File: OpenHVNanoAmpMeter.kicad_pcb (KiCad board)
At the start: 2 copper layers, 7 parts, among them U1 DDC112U

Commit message: started some layouting
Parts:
- added J1: Conn_Coaxial, Connector_Coaxial:SMA_Amphenol_132289_EdgeMount, F.Cu at (56.2, 61.9)
- added J2: Conn_Coaxial, Connector_Coaxial:SMA_Amphenol_132289_EdgeMount, F.Cu at (56.2, 42.9)
- added J3: AVR-ISP-6, Connector_PinHeader_2.54mm:PinHeader_2x03_P2.54mm_Vertical_SMD, F.Cu at (100.0, 57.0)
- added R1: R, Resistor_SMD:R_0603_1608Metric, F.Cu at (60.9, 59.9)
- added R2: R, Resistor_SMD:R_0603_1608Metric, F.Cu at (60.9, 44.9)
- added R3: 4k7, Resistor_SMD:R_0603_1608Metric, F.Cu at (94.3, 62.7)
- added R4: 4k7, Resistor_SMD:R_0402_1005Metric, F.Cu at (104.8, 69.0)
- added R5: 4k7, Resistor_SMD:R_0402_1005Metric, F.Cu at (104.8, 68.1)
- added R6: 4k7, Resistor_SMD:R_0402_1005Metric, F.Cu at (104.8, 70.0)
- added R7: 4k7, Resistor_SMD:R_0402_1005Metric, F.Cu at (104.8, 67.1)
- added U2: ATmega328PB-M, Package_DFN_QFN:QFN-32-1EP_5x5mm_P0.5mm_EP3.1x3.1mm, F.Cu at (92.3, 45.8)
- added U3: 74LV8154, Package_SO:TSSOP-20_4.4x6.5mm_P0.65mm, F.Cu at (99.0, 66.9)
- added U4: 74LS151, Package_SO:SO-16_3.9x9.9mm_P1.27mm, F.Cu at (87.8, 65.3)
- added X1: ASCO, Oscillator:Oscillator_SMD_Abracon_ASCO-4Pin_1.6x1.2mm, F.Cu at (105.0, 65.5)
- moved C4 146.4 mm to (64.1, 45.9), turned to 180 degrees
- moved C3 145.0 mm to (66.6, 45.9), turned to 180 degrees
- moved U1 135.1 mm to (69.2, 52.4), turned to 90 degrees
- moved C2 129.9 mm to (64.1, 58.9), turned to 0 degrees
- moved C1 128.3 mm to (66.6, 58.9), turned to 0 degrees
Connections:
- U1 pad 1: /CurrentMeasurement/IN1 -> Net-(R1-Pad2)
- U1 pad 10: unconnected-(U1-Pad10) -> /Clock Generation/CLK_10MHz
- U1 pad 11: unconnected-(U1-Pad11) -> /CurrentMeasurement/DCLK
- U1 pad 12: unconnected-(U1-Pad12) -> /CurrentMeasurement/DXMIT
- U1 pad 13: unconnected-(U1-Pad13) -> /CurrentMeasurement/DIN
- U1 pad 16: unconnected-(U1-Pad16) -> /CurrentMeasurement/DOUT
- U1 pad 17: unconnected-(U1-Pad17) -> /CurrentMeasurement/DVALID
- U1 pad 18: unconnected-(U1-Pad18) -> /CurrentMeasurement/RANGE0
- U1 pad 19: unconnected-(U1-Pad19) -> /CurrentMeasurement/RANGE1
- U1 pad 20: unconnected-(U1-Pad20) -> /CurrentMeasurement/RANGE2
- U1 pad 22: unconnected-(U1-Pad22) -> /CurrentMeasurement/VREF
- U1 pad 28: /CurrentMeasurement/IN2 -> Net-(R2-Pad2)
- U1 pad 8: unconnected-(U1-Pad8) -> /CurrentMeasurement/TEST
- U1 pad 9: unconnected-(U1-Pad9) -> /Clock Generation/CONV
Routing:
- net /Clock Generation/BIT3: track 0.00 -> 11.8 mm, vias 0 -> 2
- net /Clock Generation/BIT2: track 0.00 -> 11.6 mm, vias 0 -> 2
- net /Clock Generation/BIT1: track 0.00 -> 11.5 mm, vias 0 -> 2
- net /Clock Generation/BIT0: track 0.00 -> 11.4 mm, vias 0 -> 2
- net /Clock Generation/BIT4: track 0.00 -> 8.55 mm
- net /Clock Generation/BIT5: track 0.00 -> 7.63 mm
- net /Clock Generation/BIT6: track 0.00 -> 6.57 mm
- net /Clock Generation/BIT7: track 0.00 -> 6.31 mm
- net /CurrentMeasurement/IN2: track 0.00 -> 5.76 mm
- net /CurrentMeasurement/IN1: track 0.00 -> 5.73 mm
- net Net-(R2-Pad2): track 0.00 -> 2.02 mm
- net Net-(R1-Pad2): track 0.00 -> 2.02 mm
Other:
- board outline added: 75.9 x 39.3 mm

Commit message: proceeded with routing
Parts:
- removed BT2: 9V, Battery:BatteryHolder_MPD_BA9VPC_1xPP3
- added C10: 10u, Capacitor_SMD:CP_Elec_4x3.9, F.Cu at (78.6, 63.3)
- added C11: 100n, Capacitor_SMD:C_0603_1608Metric, F.Cu at (76.8, 59.1)
- added C12: 100n, Capacitor_SMD:C_0603_1608Metric, F.Cu at (85.1, 56.3)
- added C13: 100n, Capacitor_SMD:C_0603_1608Metric, F.Cu at (83.6, 56.3)
- added C14: 100n, Capacitor_SMD:C_0603_1608Metric, F.Cu at (85.4, 46.3)
- added C15: 100n, Capacitor_SMD:C_0603_1608Metric, F.Cu at (93.9, 71.0)
- added C16: 100n, Capacitor_SMD:C_0603_1608Metric, F.Cu at (82.9, 71.0)
- added C17: 100n, Capacitor_SMD:C_0603_1608Metric, F.Cu at (104.6, 70.6)
- added C5: 10u, Capacitor_SMD:CP_Elec_4x3.9, F.Cu at (81.5, 15.4)
- added C6: 100n, Capacitor_SMD:C_0603_1608Metric, F.Cu at (79.2, 19.0)
- added C7: 470n, Capacitor_SMD:C_0603_1608Metric, F.Cu at (71.1, 17.4)
- added C8: 10u, Capacitor_SMD:CP_Elec_4x3.9, F.Cu at (68.6, 63.3)
- added C9: 100n, Capacitor_SMD:C_0603_1608Metric, F.Cu at (69.4, 59.1)
- added R8: 10k, Resistor_SMD:R_0603_1608Metric, F.Cu at (77.0, 18.2)
- added U5: REF3040, Package_TO_SOT_SMD:SOT-23, F.Cu at (73.7, 17.2)
- BT1: moved to B.Cu
- moved BT1 58.6 mm to (113.8, 45.8), turned to 180 degrees
- moved J3 14.4 mm to (95.3, 43.4)
- moved U2 8.99 mm to (85.1, 51.3), turned to -90 degrees
- moved X1 5.63 mm to (101.9, 70.2)
- moved R4 3.33 mm to (101.7, 67.8)
- moved R5 3.33 mm to (101.7, 66.8)
- moved R6 3.33 mm to (101.7, 68.7)
- moved R7 3.33 mm to (101.7, 65.8)
- moved R3 2.98 mm to (91.4, 62.5)
- moved U4 2.98 mm to (84.8, 65.0)
- moved U3 2.98 mm to (96.1, 66.6)
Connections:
- BT1 pad 2: Net-(BT1-Pad2) -> unconnected-(BT1-Pad2)
- J3 pad 2: unconnected-(J3-Pad2) -> +5VD
- R6 pad 1: Net-(R6-Pad1) -> +5VD
- R7 pad 1: Net-(R6-Pad1) -> +5VD
- U1 pad 13: /CurrentMeasurement/DIN -> GND
- U1 pad 14: unconnected-(U1-Pad14) -> +5VD
- U1 pad 7: unconnected-(U1-Pad7) -> +5VA
- U2 pad 18: Net-(U2-Pad18) -> +5VD
- U2 pad 20: Net-(U2-Pad18) -> +5VD
- U2 pad 22: /CurrentMeasurement/DIN -> unconnected-(U2-Pad22)
- U2 pad 4: Net-(U2-Pad18) -> +5VD
- U3 pad 20: unconnected-(U3-Pad20) -> +5VD
- U4 pad 16: unconnected-(U4-Pad16) -> +5VD
- X1 pad 4: unconnected-(X1-Pad4) -> +5VD
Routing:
- net /Clock Generation/MUX_S0: track 0.00 -> 28.3 mm, vias 0 -> 2
- net /Clock Generation/MUX_S1: track 0.00 -> 25.7 mm, vias 0 -> 2
- net /Clock Generation/MUX_S2: track 0.00 -> 23.3 mm, vias 0 -> 2
- net +5VD: track 0.00 -> 22.7 mm, vias 0 -> 2
- net /Clock Generation/CONV: track 0.00 -> 16.9 mm
- net /CurrentMeasurement/RANGE2: track 0.00 -> 13.8 mm
- net /CurrentMeasurement/RANGE1: track 0.00 -> 12.3 mm
- net /Clock Generation/CLK_10MHz: track 0.00 -> 11.7 mm, vias 0 -> 1
- net /DataProcessing/~{RESET}: track 0.00 -> 10.8 mm
- net /CurrentMeasurement/RANGE0: track 0.00 -> 10.6 mm
- net /DataProcessing/SCL: track 0.00 -> 7.85 mm
- net /DataProcessing/SDA: track 0.00 -> 7.74 mm
- net /DataProcessing/TXD0: track 0.00 -> 7.41 mm
- net /DataProcessing/RXD0: track 0.00 -> 7.35 mm
- net +5VA: track 0.00 -> 5.13 mm
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- added copper zone on B.Cu, net GND
- added copper zone on F.Cu, net GND
- added copper zone on B.Cu, net GNDA
- added copper zone on F.Cu, net GNDA
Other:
- board size 75.9 x 39.3 mm -> 64.5 x 38 mm
- board text added: "IN1"
- board text added: "IN2"

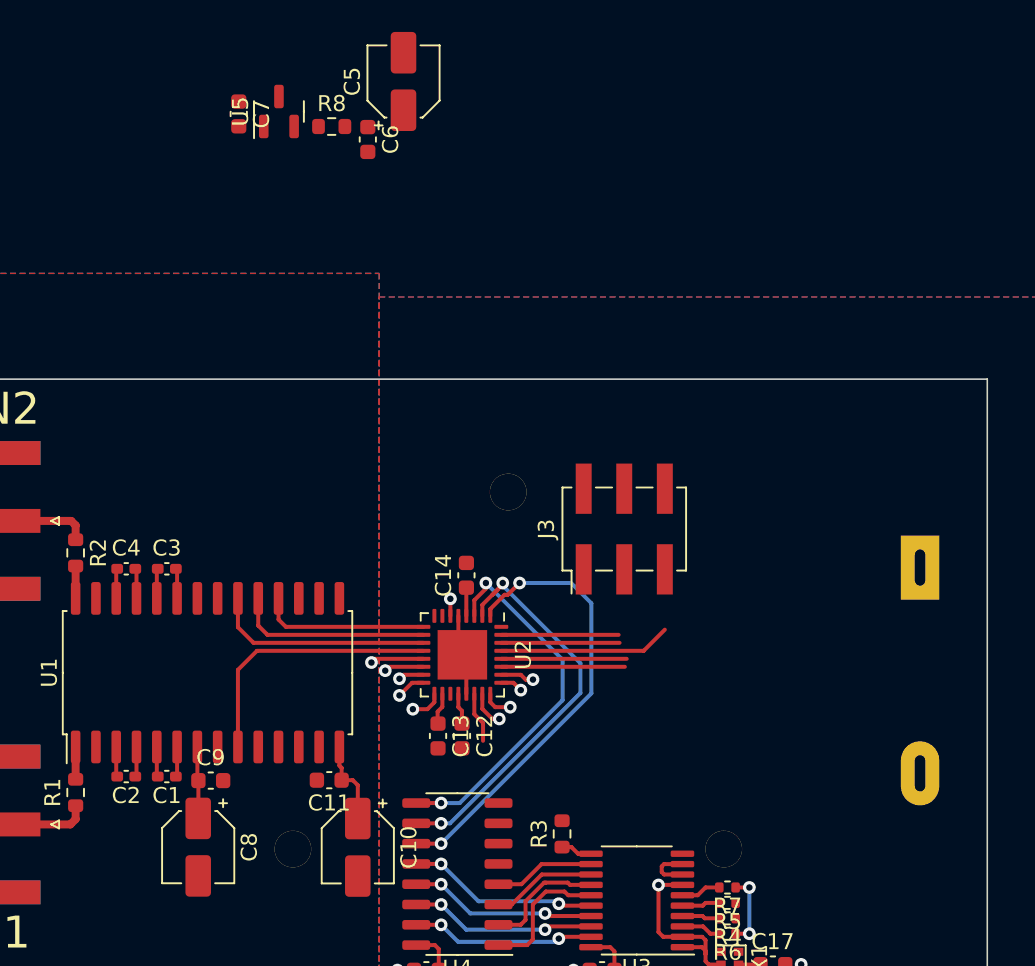
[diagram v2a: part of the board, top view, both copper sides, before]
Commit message: ISP connection routed
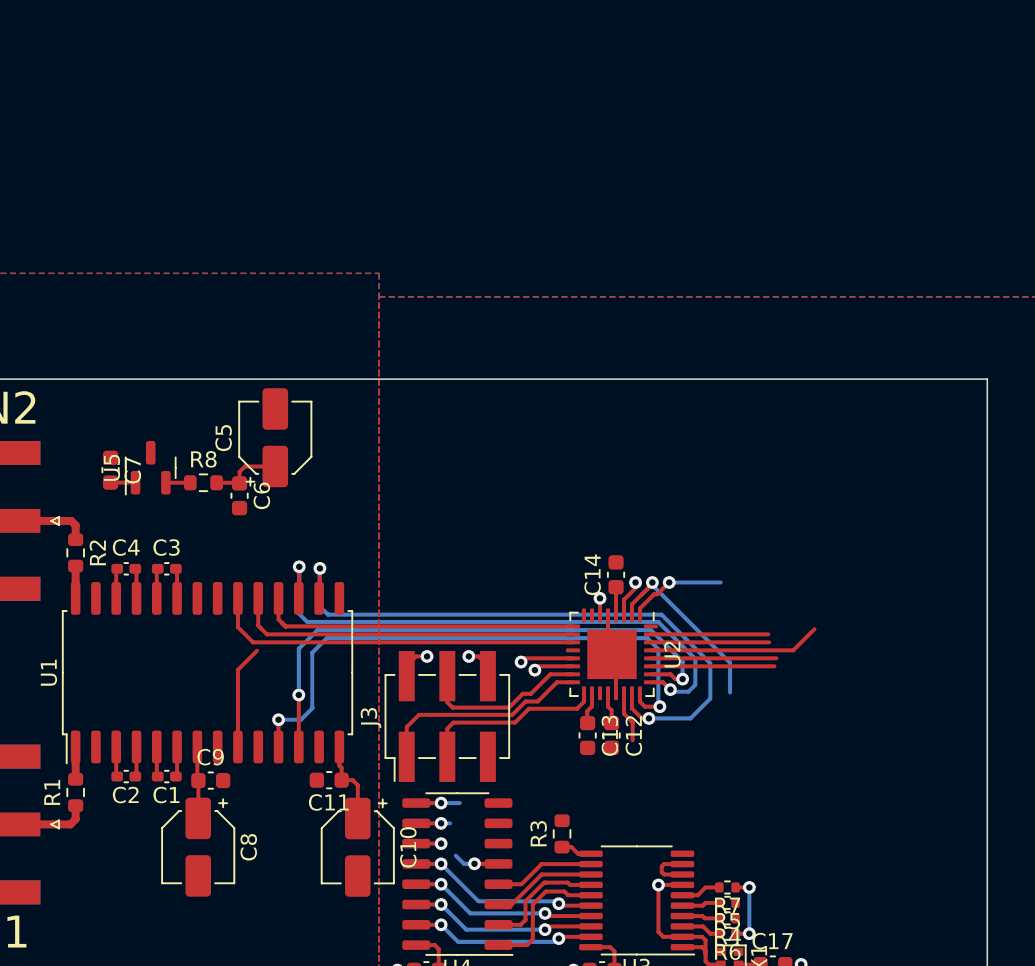
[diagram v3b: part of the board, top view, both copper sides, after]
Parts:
- removed BT1: 9V, Battery:BatteryHolder_MPD_BA9VPC_1xPP3
- moved R8 23.7 mm to (68.9, 40.5)
- moved C5 23.7 mm to (73.4, 37.7)
- moved C6 23.7 mm to (71.2, 41.3)
- moved C7 23.7 mm to (63.1, 39.7)
- moved U5 23.7 mm to (65.6, 39.5)
- moved J3 16.1 mm to (84.2, 55.1)
- moved C12 9.37 mm to (94.5, 56.3)
- moved C13 9.37 mm to (93.0, 56.3)
- moved C14 9.37 mm to (94.8, 46.2)
- moved U2 9.37 mm to (94.5, 51.2)
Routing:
- net /CurrentMeasurement/DOUT: track 2.27 -> 39.0 mm, vias 1 -> 2
- net /CurrentMeasurement/DVALID: track 1.41 -> 35.7 mm, vias 1 -> 2
- net /CurrentMeasurement/DCLK: track 1.91 -> 35.5 mm, vias 1 -> 2
- net /CurrentMeasurement/DXMIT: track 2.11 -> 35.3 mm, vias 1 -> 2
- net /Clock Generation/MUX_S0: track 28.3 -> 7.54 mm
- net /Clock Generation/MUX_S2: track 23.3 -> 4.91 mm
- net /Clock Generation/MUX_S1: track 25.7 -> 14.0 mm
- net /DataProcessing/MISO: track 1.83 -> 13.4 mm, vias 1 -> 0
- net /CurrentMeasurement/RANGE0: track 10.6 -> 20.3 mm
- net /DataProcessing/SCK: track 2.06 -> 11.5 mm, vias 1 -> 0
- net /CurrentMeasurement/RANGE2: track 13.8 -> 23.2 mm
- net /CurrentMeasurement/RANGE1: track 12.3 -> 21.6 mm
- net /DataProcessing/MOSI: track 1.60 -> 10.5 mm, vias 1 -> 0
- net /Clock Generation/CONV: track 16.9 -> 9.39 mm, vias 0 -> 1
- net Net-(C5-Pad1): track 0.00 -> 4.55 mm
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
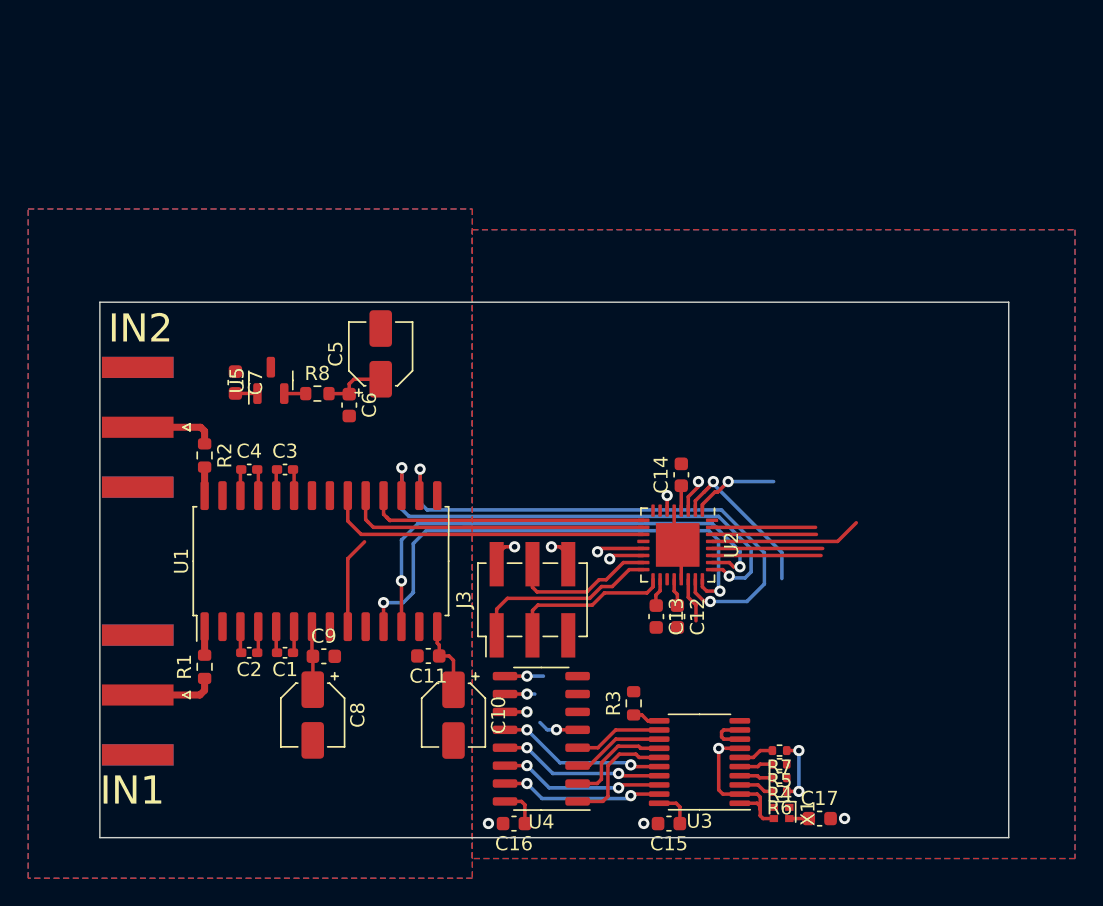
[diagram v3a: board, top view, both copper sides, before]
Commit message: implemented linear regulators
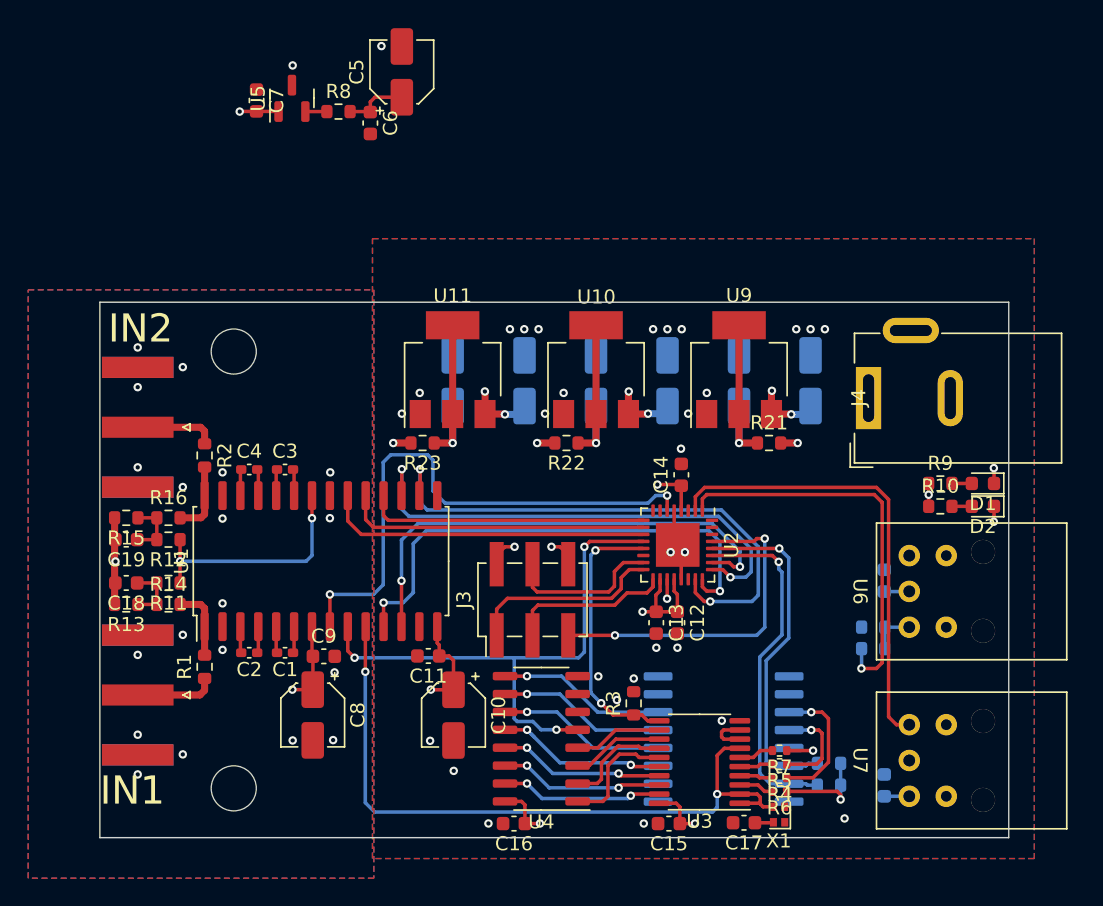
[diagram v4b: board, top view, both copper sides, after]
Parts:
- added C18: 1u, Capacitor_SMD:C_0603_1608Metric, F.Cu at (55.4, 53.9)
- added C19: 1u, Capacitor_SMD:C_0603_1608Metric, F.Cu at (55.4, 50.9)
- added C20: 100n, Capacitor_SMD:C_0603_1608Metric, B.Cu at (109.2, 53.8)
- added C21: 100n, Capacitor_SMD:C_0603_1608Metric, B.Cu at (109.2, 68.3)
- added C22: 10u, Capacitor_SMD:CP_Elec_4x3.9, B.Cu at (83.6, 39.6)
- added C23: 10u, Capacitor_SMD:CP_Elec_4x3.9, B.Cu at (103.9, 39.6)
- added C24: 10u, Capacitor_SMD:CP_Elec_4x3.9, B.Cu at (93.8, 39.6)
- added C25: 10u, Capacitor_SMD:CP_Elec_4x3.9, B.Cu at (98.9, 39.6)
- added C26: 10u, Capacitor_SMD:CP_Elec_4x3.9, B.Cu at (88.7, 39.6)
- added C27: 10u, Capacitor_SMD:CP_Elec_4x3.9, B.Cu at (78.5, 39.6)
- added D1: LED, LED_SMD:LED_0603_1608Metric, F.Cu at (116.2, 46.9)
- added D2: LED, LED_SMD:LED_0603_1608Metric, F.Cu at (116.2, 48.5)
- added H1: MountingHole, MountingHole:MountingHole_3.2mm_M3_DIN965, F.Cu at (63.0, 37.5)
- added H2: MountingHole, MountingHole:MountingHole_3.2mm_M3_DIN965, F.Cu at (63.0, 68.5)
- added J4: Barrel_Jack_Switch, Connector_BarrelJack:BarrelJack_Wuerth_6941xx301002, F.Cu at (108.1, 40.8)
- added R10: R, Resistor_SMD:R_0603_1608Metric, F.Cu at (113.1, 48.5)
- added R11: R, Resistor_SMD:R_0603_1608Metric, F.Cu at (58.4, 53.9)
- added R12: R, Resistor_SMD:R_0603_1608Metric, F.Cu at (58.4, 50.9)
- added R13: R, Resistor_SMD:R_0603_1608Metric, F.Cu at (55.4, 55.4)
- added R14: R, Resistor_SMD:R_0603_1608Metric, F.Cu at (58.4, 55.4)
- added R15: R, Resistor_SMD:R_0603_1608Metric, F.Cu at (55.4, 49.3)
- added R16: R, Resistor_SMD:R_0603_1608Metric, F.Cu at (58.4, 49.3)
- added R17: R, Resistor_SMD:R_0603_1608Metric, B.Cu at (108.4, 58.6)
- added R18: R, Resistor_SMD:R_0603_1608Metric, B.Cu at (108.4, 57.1)
- added R19: 4k7, Resistor_SMD:R_0603_1608Metric, B.Cu at (105.2, 66.7)
- added R20: 4k7, Resistor_SMD:R_0603_1608Metric, B.Cu at (105.2, 68.3)
- added R21: R, Resistor_SMD:R_0603_1608Metric, F.Cu at (101.0, 44.0)
- added R22: R, Resistor_SMD:R_0603_1608Metric, F.Cu at (86.6, 44.0)
- added R23: R, Resistor_SMD:R_0603_1608Metric, F.Cu at (76.4, 44.0)
- added R9: R, Resistor_SMD:R_0603_1608Metric, F.Cu at (113.1, 46.9)
- added U10: NCP1117-5.0_SOT223, Package_TO_SOT_SMD:SOT-223-3_TabPin2, F.Cu at (88.7, 38.8)
- added U11: NCP1117-5.0_SOT223, Package_TO_SOT_SMD:SOT-223-3_TabPin2, F.Cu at (78.5, 38.8)
- added U6: TOTX147PL, toslink:TOTX147PL, F.Cu at (113.6, 54.5)
- added U7: TORX147PL, toslink:TORX147PL, F.Cu at (113.6, 66.5)
- added U8: PCF8574, Package_SO:SOIC-16W_7.5x10.3mm_P1.27mm, B.Cu at (97.8, 65.0)
- added U9: NCP1117-3.3_SOT223, Package_TO_SOT_SMD:SOT-223-3_TabPin2, F.Cu at (98.9, 38.8)
- moved C6 20.1 mm to (72.7, 21.3)
- moved C7 20.1 mm to (64.6, 19.7)
- moved U5 20.1 mm to (67.1, 19.5)
- moved C5 20.1 mm to (74.9, 17.7)
- moved R8 20.1 mm to (70.4, 20.5)
- moved C17 5.38 mm to (99.2, 70.9), turned to 180 degrees
- moved C12 0.44 mm to (94.5, 56.7)
- moved C13 0.44 mm to (93.0, 56.7)
- moved X1 0.21 mm to (101.7, 70.4), turned to 180 degrees
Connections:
- net Net-(R1-Pad2) renamed /CurrentMeasurement/IN1_INP
- net Net-(R2-Pad2) renamed /CurrentMeasurement/IN2_INP
- U2 pad 1: /Clock Generation/MUX_S0 -> /DataProcessing/LWLTX
- U2 pad 13: /Clock Generation/CNT_AU -> /Clock Generation/CNT_CLR
- U2 pad 14: /Clock Generation/CNT_BL -> unconnected-(U2-Pad14)
- U2 pad 19: unconnected-(U2-Pad19) -> Net-(D2-Pad1)
- U2 pad 2: /Clock Generation/MUX_S1 -> /DataProcessing/LWLRX
- U2 pad 22: unconnected-(U2-Pad22) -> Net-(D1-Pad1)
- U2 pad 3: /Clock Generation/MUX_S2 -> unconnected-(U2-Pad3)
- U2 pad 32: /Clock Generation/CNT_CLR -> unconnected-(U2-Pad32)
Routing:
- net /CurrentMeasurement/TEST: track 1.07 -> 39.4 mm, vias 1 -> 2
- net /Clock Generation/CLK_10MHz: track 11.7 -> 49.5 mm, vias 1 -> 2
- net /DataProcessing/LWLRX: track 0.00 -> 32.5 mm
- net /Clock Generation/CONV: track 9.39 -> 39.8 mm, vias 1 -> 3
- net /DataProcessing/LWLTX: track 0.00 -> 28.4 mm, vias 0 -> 1
- net /Clock Generation/CNT_CLR: track 1.98 -> 19.4 mm, vias 0 -> 2
- net /DataProcessing/SDA: track 7.74 -> 25.1 mm, vias 0 -> 1
- net /CurrentMeasurement/VREF: track 0.00 -> 16.9 mm, vias 0 -> 2
- net /DataProcessing/SCL: track 7.85 -> 24.7 mm, vias 0 -> 1
- net +3V3: track 0.00 -> 16.7 mm, vias 0 -> 1
- net +5VD: track 24.8 -> 38.8 mm, vias 3 -> 10
- net /DataProcessing/~{RESET}: track 10.8 -> 24.3 mm, vias 0 -> 2
- net /Power Supply/VIN: track 0.00 -> 13.2 mm, vias 0 -> 6
- net Net-(U11-Pad2): track 0.00 -> 12.3 mm, vias 0 -> 1
- net Net-(U9-Pad2): track 0.00 -> 12.3 mm, vias 0 -> 1
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- added copper zone on In2.Cu, net +3V3
- added copper zone on In2.Cu, net +5VA
- added copper zone on In2.Cu, net +5VD
- added copper zone on In2.Cu, net /Power Supply/VIN
- added copper zone on In1.Cu, net GND
- added copper zone on In2.Cu, net GND
- added copper zone on In1.Cu, net GNDA
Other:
- copper layers 2 -> 4
